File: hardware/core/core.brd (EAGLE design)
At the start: 159.7 x 163.8 mm, 549 parts, among them IC1 MAX481CSA, IC10 MAX481CSA, IC11 MAX481CSA, IC12 MAX481CSA, IC13 MAX481CSA, IC14 MAX481CSA, IC15 MAX481CSA, IC16 MAX481CSA, IC17 MAX481CSA, IC18 MAX481CSA, IC19 MAX481CSA, IC2 LD117AS12TR, IC20 MAX481CSA, IC21 MAX481CSA, IC22 LD117AS12TR, IC23 LD117AS12TR, IC3 MAX481CSA, IC4 MAX481CSA, IC5 MAX481CSA, IC6 MAX481CSA, IC7 MAX481CSA, IC8 MAX481CSA, IC9 MAX481CSA

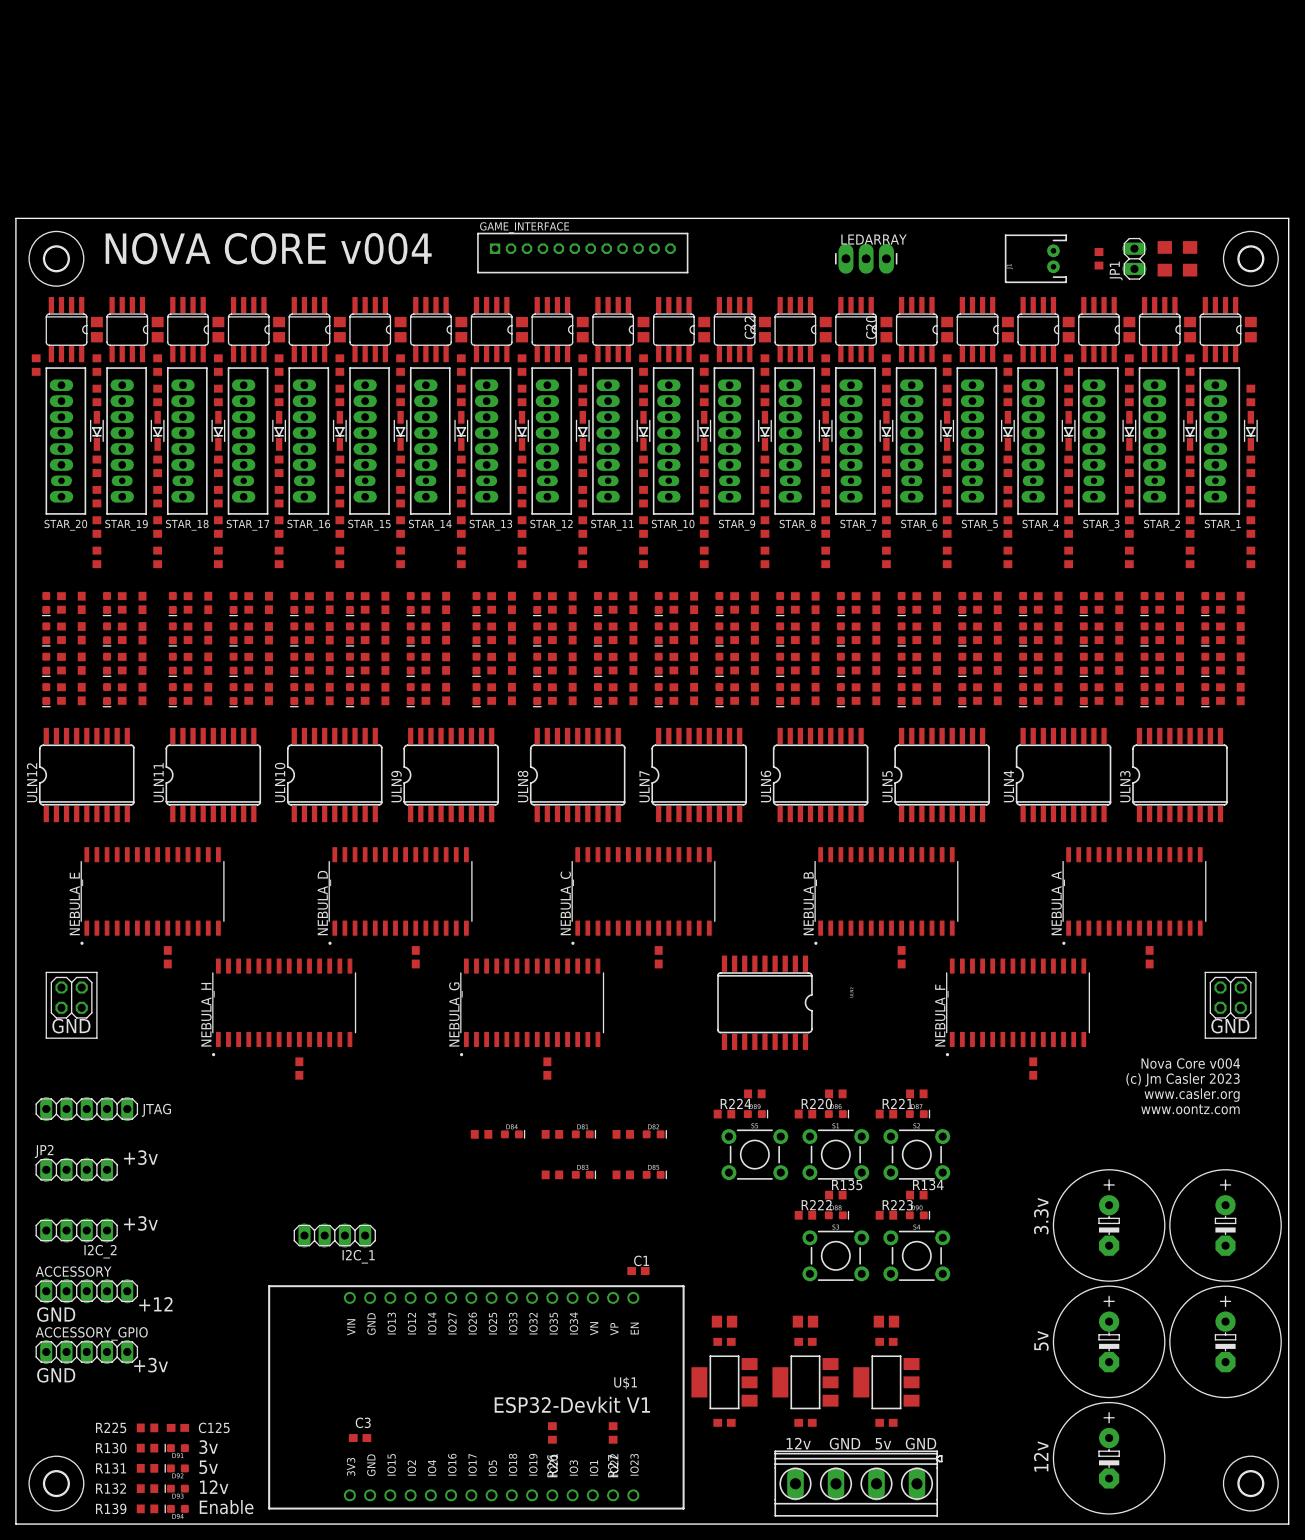
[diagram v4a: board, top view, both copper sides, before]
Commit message: Add TVS and change led resistors to 1k
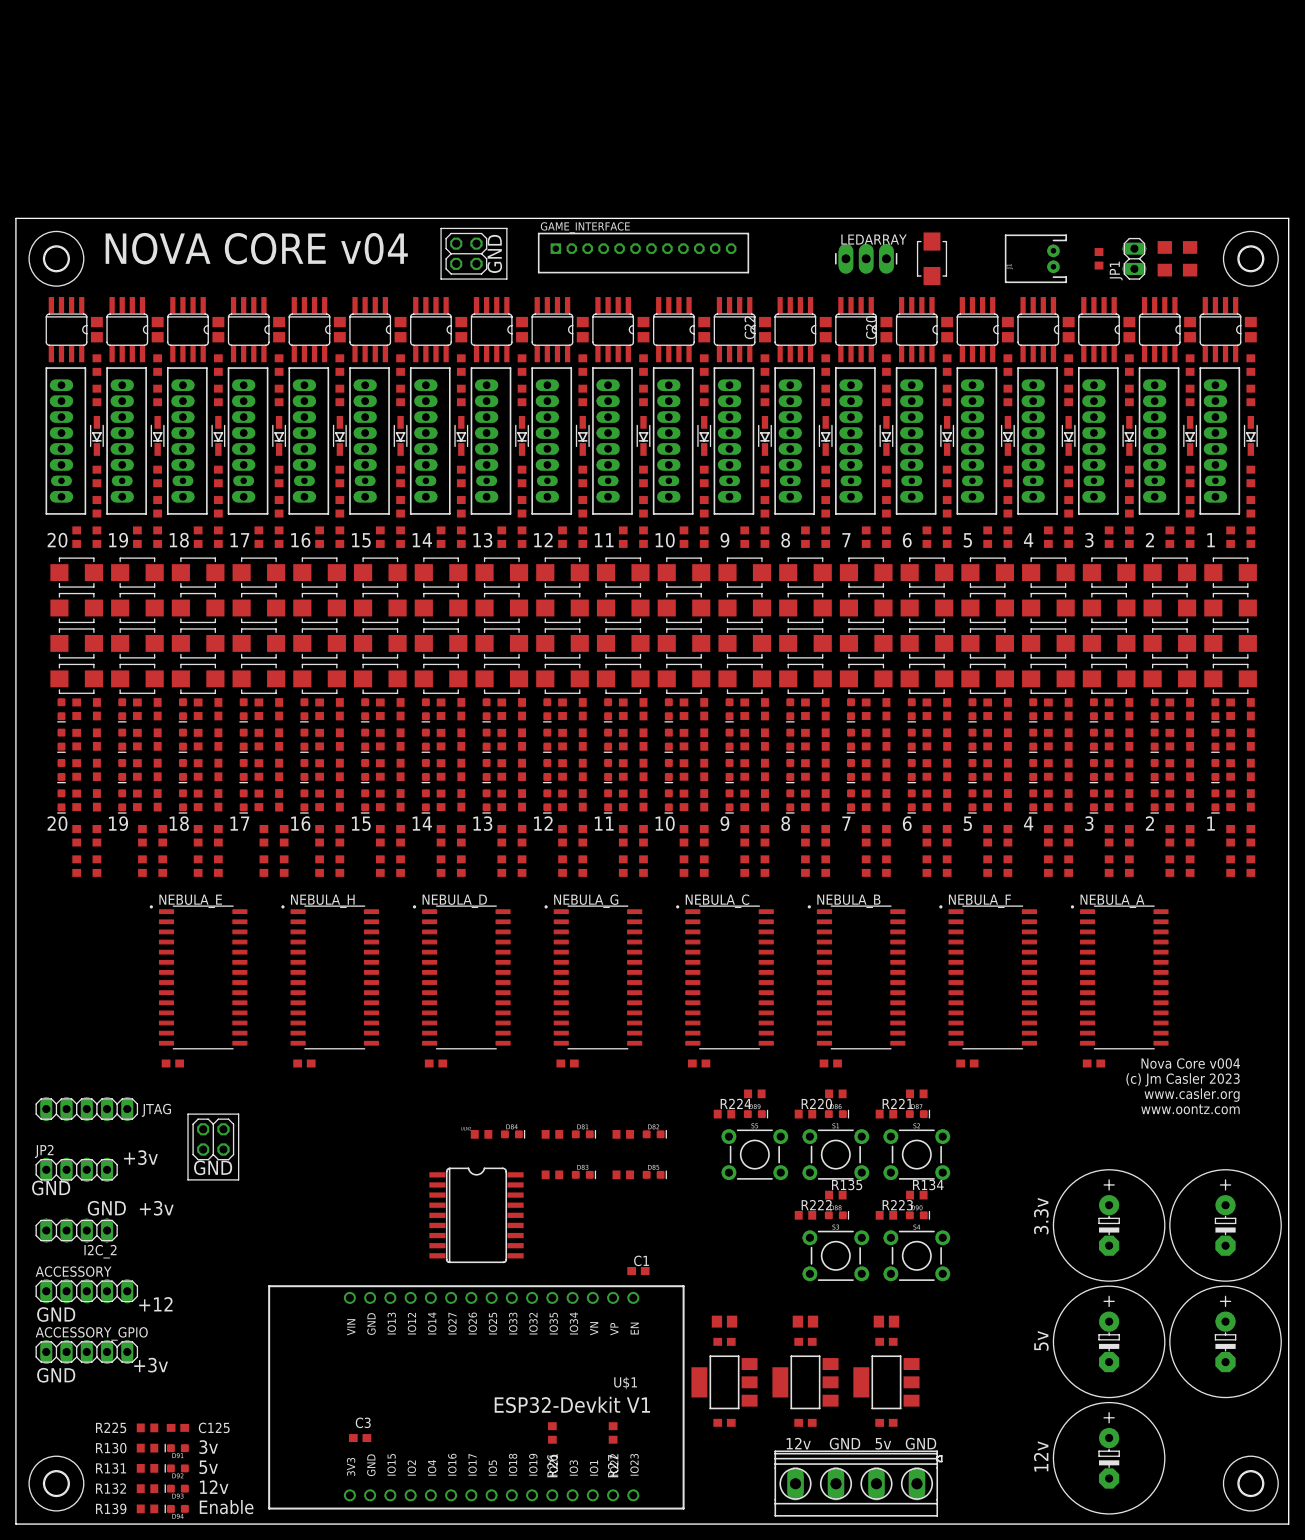
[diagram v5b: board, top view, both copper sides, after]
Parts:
- removed I2C_1: (no value), pinhead:1X04
- removed ULN10, ULN11, ULN12, ULN3, ULN4, ULN5, ULN6, ULN7, ULN8, ULN9: (no value), SparkFun-IC-Special-Function:SO18L
- added D115, D116, D117, D118, D119, D120, D121, D122, D123, D124, D125, D126, D127, D128, D129, D130, D131, D132, D133, D134, D135, D136, D137, D138, D139, D140, D141, D142, D143, D144, D145, D146, D147, D148, D149, D150, D151, D152, D153, D154, D155, D156, D157, D158, D159, D160, D161, D162, D163, D164, D165, D166, D167, D168, D169, D170, D171, D172, D173, D174, D175, D176, D177, D178, D179, D180, D181, D182, D183, D184, D185, D186, D187, D188, D189, D190, D191, D192, D193, D194, D195: SMBJ8.0CA, SMBJ8.0CA:DIOM4336X265N
- added R226, R227, R228, R229, R230, R231, R232, R233, R234, R235, R236, R237, R238, R239, R240, R241, R242, R243, R244, R245, R246, R247, R248, R249, R250, R251, R252, R253, R254, R255, R256, R257, R258, R259, R260, R261, R262, R263, R264, R265, R266, R267, R268, R269, R270, R271, R272, R273, R274, R275, R276, R277, R278, R279, R280, R281, R282, R283, R284, R285, R286, R287, R288, R289, R290, R291, R292, R293, R294, R295, R296, R297, R298, R299, R300, R301, R302, R303, R304, R305: 68, rcl:R0603
- R10, R100, R101, R102, R11, R12, R13, R14, R15, R16, R17, R18, R19, R20, R21, R22, R23, R24, R25, R28, R29, R3, R30, R31, R32, R33, R34, R35, R36, R37, R38, R39, R4, R40, R41, R42, R43, R44, R45, R46, R47, R48, R49, R5, R50, R51, R52, R53, R6, R66, R69, R7, R70, R71, R72, R73, R74, R75, R76, R77, R78, R79, R8, R80, R81, R82, R87, R88, R89, R9, R90, R91, R92, R93, R94, R95, R96, R97, R98, R99: value 10k -> 1k
- moved JP3 133.8 mm to (56.5, 159.4), turned to 90 degrees
- moved ULN2 46.3 mm to (57.8, 43.2), turned to 270 degrees
- moved JP4 25.1 mm to (24.8, 48.3)
- moved C10 16.0 mm to (102.2, 57.8), turned to 180 degrees
- moved NEBULA_C 15.3 mm to (89.5, 68.6), turned to 0 degrees
- moved C8 15.1 mm to (135.3, 57.8), turned to 180 degrees
- moved C9 14.3 mm to (85.7, 57.8), turned to 180 degrees
- moved NEBULA_D 13.6 mm to (56.5, 68.6), turned to 0 degrees
- moved C11 13.6 mm to (52.7, 57.8), turned to 180 degrees
- moved C102 13.5 mm to (55.9, 94.6)
- moved C103 13.5 mm to (55.9, 98.4)
- moved C118 13.5 mm to (17.8, 94.6)
- moved C119 13.5 mm to (17.8, 98.4)
- moved C122 13.5 mm to (10.2, 94.6)
- moved C123 13.5 mm to (10.2, 98.4)
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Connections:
- new net N$345: C45.1, D123.2, R11.1, R151.1, R234.2
- net +12V: no longer ULN10.10, ULN11.10, ULN12.10, ULN3.10, ULN4.10, ULN5.10, ULN6.10, ULN7.10, ULN8.10, ULN9.10
- net +3V3: no longer I2C_1.1
- net +5V: no longer D1.A, D10.A, D11.A, D12.A, D13.A, D14.A, D15.A, D16.A, D17.A, D18.A, D19.A, D2.A, D20.A, D21.A, D22.A, D23.A, D24.A, D25.A, D26.A, D27.A, D28.A, D29.A, D3.A, D30.A, D31.A, D32.A, D33.A, D34.A, D35.A, D36.A, D37.A, D38.A, D39.A, D4.A, D40.A, D41.A, D42.A, D43.A, D44.A, D45.A, D46.A, D47.A, D48.A, D49.A, D5.A, D50.A, D51.A, D52.A, D53.A, D54.A, D55.A, D56.A, D57.A, D58.A, D59.A, D6.A, D60.A, D61.A, D62.A, D63.A, D64.A, D65.A, D66.A, D67.A, D68.A, D69.A, D7.A, D70.A, D71.A, D72.A, D73.A, D74.A, D75.A, D76.A, D77.A, D78.A, D79.A, D8.A, D80.A, D9.A
- net 21/SDA: no longer I2C_1.4
- net 22/SCL: no longer I2C_1.3
- net A0: now also R226.1; no longer ULN3.8
- net A1: now also R227.1; no longer ULN3.7
- net A10: now also R236.1; no longer ULN4.6
- net A11: now also R237.1; no longer ULN4.5
- net A12: now also R238.1; no longer ULN4.4
- net A13: now also R239.1; no longer ULN4.3
- net A14: now also R240.1; no longer ULN4.2
- net A15: now also R241.1; no longer ULN4.1
- net A2: now also R228.1; no longer ULN3.6
- net A3: now also R229.1; no longer ULN3.5
- net A4: now also R230.1; no longer ULN3.4
- net A5: now also R231.1; no longer ULN3.3
- net A6: now also R232.1; no longer ULN3.2
- net A7: now also R233.1; no longer ULN3.1
- net A8: now also R234.1; no longer ULN4.8
- net A9: now also R235.1; no longer ULN4.7
- net B0: now also R242.1; no longer ULN5.8
- net B1: now also R243.1; no longer ULN5.7
- net B10: now also R252.1; no longer ULN6.6
- net B11: now also R253.1; no longer ULN6.5
- net B12: now also R254.1; no longer ULN6.4
- net B13: now also R255.1; no longer ULN6.3
- net B14: now also R256.1; no longer ULN6.2
- net B15: now also R257.1; no longer ULN6.1
- net B2: now also R244.1; no longer ULN5.6
- net B3: now also R245.1; no longer ULN5.5
- net B4: now also R246.1; no longer ULN5.4
- net B5: now also R247.1; no longer ULN5.3
- net B6: now also R248.1; no longer ULN5.2
- net B7: now also R249.1; no longer ULN5.1
- net B8: now also R250.1; no longer ULN6.8
- net B9: now also R251.1; no longer ULN6.7
- net C0: now also R258.1; no longer ULN7.8
- net C1: now also R259.1; no longer ULN7.7
- net C10: now also R268.1; no longer ULN8.6
- net C11: now also R269.1; no longer ULN8.5
- net C12: now also R270.1; no longer ULN8.4
- net C13: now also R271.1; no longer ULN8.3
- net C14: now also R272.1; no longer ULN8.2
- net C15: now also R273.1; no longer ULN8.1
- net C2: now also R260.1; no longer ULN7.6
- net C3: now also R261.1; no longer ULN7.5
- net C4: now also R262.1; no longer ULN7.4
- net C5: now also R263.1; no longer ULN7.3
- net C6: now also R264.1; no longer ULN7.2
- net C7: now also R265.1; no longer ULN7.1
- net C8: now also R266.1; no longer ULN8.8
- net C9: now also R267.1; no longer ULN8.7
- net D0: now also R274.1; no longer ULN9.8
- net D1: now also R275.1; no longer ULN9.7
- net D10: now also R284.1; no longer ULN10.6
- net D11: now also R285.1; no longer ULN10.5
- net D12: now also R286.1; no longer ULN10.4
- net D13: now also R287.1; no longer ULN10.3
- net D14: now also R288.1; no longer ULN10.2
- net D15: now also R289.1; no longer ULN10.1
- net D2: now also R276.1; no longer ULN9.6
- net D3: now also R277.1; no longer ULN9.5
- net D4: now also R278.1; no longer ULN9.4
- net D5: now also R279.1; no longer ULN9.3
- net D6: now also R280.1; no longer ULN9.2
- net D7: now also R281.1; no longer ULN9.1
- net D8: now also R282.1; no longer ULN10.8
- net D9: now also R283.1; no longer ULN10.7
- net E0: now also R290.1; no longer ULN11.8
- net E1: now also R291.1; no longer ULN11.7
- net E10: now also R300.1; no longer ULN12.6
- net E11: now also R301.1; no longer ULN12.5
- net E12: now also R302.1; no longer ULN12.4
- net E13: now also R303.1; no longer ULN12.3
- net E14: now also R304.1; no longer ULN12.2
- net E15: now also R305.1; no longer ULN12.1
- net E2: now also R292.1; no longer ULN11.6
- net E3: now also R293.1; no longer ULN11.5
- net E4: now also R294.1; no longer ULN11.4
- net E5: now also R295.1; no longer ULN11.3
- net E6: now also R296.1; no longer ULN11.2
- net E7: now also R297.1; no longer ULN11.1
- net E8: now also R298.1; no longer ULN12.8
- net E9: now also R299.1; no longer ULN12.7
- net GND: now also D10.C, D11.C, D115.1, D116.1, D117.1, D118.1, D119.1, D12.C, D120.1, D121.1, D122.1, D123.1, D124.1, D125.1, D126.1, D127.1, D128.1, D129.1, D13.C, D130.1, D131.1, D132.1, D133.1, D134.1, D135.1, D136.1, D137.1, D138.1, D139.1, D14.C, D140.1, D141.1, D142.1, D143.1, D144.1, D145.1, D146.1, D147.1, D148.1, D149.1, D15.C, D150.1, D151.1, D152.1, D153.1, D154.1, D155.1, D156.1, D157.1, D158.1, D159.1, D16.C, D160.1, D161.1, D162.1, D163.1, D164.1, D165.1, D166.1, D167.1, D168.1, D169.1, D17.C, D170.1, D171.1, D172.1, D173.1, D174.1, D175.1, D176.1, D177.1, D178.1, D179.1, D18.C, D180.1, D181.1, D182.1, D183.1, D184.1, D185.1, D186.1, D187.1, D188.1, D189.1, D19.C, D190.1, D191.1, D192.1, D193.1, D194.1, D195.1, D2.C, D20.C, D21.C, D22.C, D23.C, D24.C, D25.C, D26.C, D27.C, D28.C, D29.C, D3.C, D30.C, D31.C, D32.C, D33.C, D34.C, D35.C, D36.C, D37.C, D38.C, D39.C, D4.C, D40.C, D41.C, D42.C, D43.C, D44.C, D45.C, D46.C, D47.C, D48.C, D49.C, D5.C, D57.C, D58.C, D59.C, D6.C, D60.C, D61.C, D62.C, D63.C, D64.C, D65.C, D66.C, D67.C, D68.C, D69.C, D7.C, D70.C, D71.C, D72.C, D73.C, D74.C, D75.C, D76.C, D77.C, D78.C, D79.C, D8.C, D80.C, D9.C; no longer I2C_1.2, ULN10.9, ULN11.9, ULN12.9, ULN3.9, ULN4.9, ULN5.9, ULN6.9, ULN7.9, ULN8.9, ULN9.9
- net N$100: now also D69.A, R91.2; no longer D77.C, R99.2
- net N$101: now also D70.A, R92.2; no longer D78.C, R100.2
- net N$102: now also D71.A, R93.2; no longer D79.C, R101.2
- net N$103: now also D72.A, R94.2; no longer D80.C, R102.2
- net N$11: now also D6.A; no longer D6.C
- net N$12: now also D7.A; no longer D7.C
- net N$13: now also D8.A; no longer D8.C
- net N$14: now also D9.A; no longer D9.C
- net N$160: now also D116.2, R226.2; no longer ULN3.11
- net N$161: now also D115.2, R227.2; no longer ULN3.12
- net N$162: now also D117.2, R228.2; no longer ULN3.13
- net N$163: now also D118.2, R229.2; no longer ULN3.14
- net N$164: now also D122.2, R233.2; no longer ULN3.18
- net N$165: now also D121.2, R232.2; no longer ULN3.17
- net N$166: now also D120.2, R231.2; no longer ULN3.16
- net N$167: now also D119.2, R230.2; no longer ULN3.15
- net N$184: now also D49.A, R52.2; no longer C45.1, R11.1, R151.1, ULN4.11
- net N$185: now also D124.2, R235.2; no longer ULN4.12
- net N$186: now also D125.2, R236.2; no longer ULN4.13
- net N$187: now also D126.2, R237.2; no longer ULN4.14
- net N$188: now also D130.2, R241.2; no longer ULN4.18
- net N$189: now also D129.2, R240.2; no longer ULN4.17
- net N$190: now also D128.2, R239.2; no longer ULN4.16
- net N$191: now also D127.2, R238.2; no longer ULN4.15
- net N$192: now also D131.2, R242.2; no longer ULN5.11
- net N$193: now also D134.2, R245.2; no longer ULN5.14
- net N$194: now also D133.2, R244.2; no longer ULN5.13
- net N$195: now also D132.2, R243.2; no longer ULN5.12
- net N$196: now also D138.2, R249.2; no longer ULN5.18
- net N$197: now also D137.2, R248.2; no longer ULN5.17
- net N$198: now also D136.2, R247.2; no longer ULN5.16
- net N$199: now also D135.2, R246.2; no longer ULN5.15
- net N$20: now also D14.A, R15.2; no longer D10.C, R11.2
- net N$21: now also D15.A, R16.2; no longer D11.C, R12.2
- net N$216: now also D139.2, R250.2; no longer ULN6.11
- net N$217: now also D140.2, R251.2; no longer ULN6.12
- net N$218: now also D141.2, R252.2; no longer ULN6.13
- net N$219: now also D142.2, R253.2; no longer ULN6.14
- net N$22: now also D16.A, R17.2; no longer D12.C, R13.2
- net N$220: now also D146.2, R257.2; no longer ULN6.18
- net N$221: now also D145.2, R256.2; no longer ULN6.17
- net N$222: now also D144.2, R255.2; no longer ULN6.16
- net N$223: now also D143.2, R254.2; no longer ULN6.15
- net N$23: now also D17.A, R18.2; no longer D13.C, R14.2
- net N$240: now also D147.2, R258.2; no longer ULN7.11
- net N$241: now also D148.2, R259.2; no longer ULN7.12
- net N$242: now also D149.2, R260.2; no longer ULN7.13
- net N$243: now also D150.2, R261.2; no longer ULN7.14
- net N$245: now also D153.2, R264.2; no longer ULN7.17
- net N$246: now also D152.2, R263.2; no longer ULN7.16
- net N$247: now also D151.2, R262.2; no longer ULN7.15
- net N$248: now also D155.2, R266.2; no longer ULN8.11
- net N$249: now also D156.2, R267.2; no longer ULN8.12
- net N$250: now also D157.2, R268.2; no longer ULN8.13
- net N$251: now also D158.2, R269.2; no longer ULN8.14
- net N$252: now also D154.2, R265.2; no longer ULN7.18
- net N$253: now also D161.2, R272.2; no longer ULN8.17
- net N$254: now also D160.2, R271.2; no longer ULN8.16
- net N$255: now also D159.2, R270.2; no longer ULN8.15
- net N$26: now also D56.A, R74.2; no longer D1.C, R53.2
- net N$260: now also D162.2, R273.2; no longer ULN8.18
- net N$27: now also D55.A, R73.2; no longer D50.C, R66.2
- net N$28: now also D13.A, R14.2; no longer D14.C, R15.2
- net N$288: now also D172.2, R282.2; no longer ULN10.11
- net N$289: now also D173.2, R283.2; no longer ULN10.12
- net N$29: now also D12.A, R13.2; no longer D15.C, R16.2
- net N$290: now also D174.2, R284.2; no longer ULN10.13
- net N$291: now also D175.2, R285.2; no longer ULN10.14
- net N$292: now also D179.2, R289.2; no longer ULN10.18
- net N$293: now also D178.2, R288.2; no longer ULN10.17
- net N$294: now also D177.2, R287.2; no longer ULN10.16
- net N$295: now also D176.2, R286.2; no longer ULN10.15
- net N$296: now also D163.2, R274.2; no longer ULN9.11
- net N$297: now also D164.2, R275.2; no longer ULN9.12
- net N$298: now also D165.2, R276.2; no longer ULN9.13
- net N$299: now also D166.2, R277.2; no longer ULN9.14
- net N$3: now also D2.A; no longer D2.C
- net N$30: now also D11.A, R12.2; no longer D16.C, R17.2
- net N$300: now also D170.2, R281.2; no longer ULN9.18
- net N$301: now also D169.2, R280.2; no longer ULN9.17
- net N$302: now also D168.2, R279.2; no longer ULN9.16
- net N$303: now also D167.2, R278.2; no longer ULN9.15
- net N$304: now also D180.2, R290.2; no longer ULN11.11
- net N$305: now also D181.2, R291.2; no longer ULN11.12
- net N$306: now also D182.2, R292.2; no longer ULN11.13
- net N$307: now also D183.2, R293.2; no longer ULN11.14
- net N$308: now also D187.2, R297.2; no longer ULN11.18
- net N$309: now also D186.2, R296.2; no longer ULN11.17
- net N$31: now also D10.A, R11.2; no longer D17.C, R18.2
- net N$310: now also D185.2, R295.2; no longer ULN11.16
- net N$311: now also D184.2, R294.2; no longer ULN11.15
- net N$312: now also D188.2, R298.2; no longer ULN12.11
- net N$313: now also D189.2, R299.2; no longer ULN12.12
- net N$314: now also D190.2, R300.2; no longer ULN12.13
- net N$315: now also D191.2, R301.2; no longer ULN12.14
- net N$316: now also D195.2, R305.2; no longer ULN12.18
- net N$317: now also D194.2, R304.2; no longer ULN12.17
- net N$318: now also D193.2, R303.2; no longer ULN12.16
- net N$319: now also D192.2, R302.2; no longer ULN12.15
- net N$32: now also D54.A, R72.2; no longer D51.C, R69.2
- net N$33: now also D53.A, R71.2; no longer D52.C, R70.2
- net N$34: now also D80.A, R102.2; no longer D65.C, R87.2
- net N$35: now also D1.A, R53.2; no longer D53.C, R71.2
- net N$36: now also D25.A, R28.2; no longer D18.C, R19.2
- net N$37: now also D24.A, R25.2; no longer D19.C, R20.2
- net N$38: now also D23.A, R24.2; no longer D20.C, R21.2
- net N$39: now also D22.A, R23.2; no longer D21.C, R22.2
- net N$4: now also D3.A; no longer D3.C
- net N$40: now also D50.A, R66.2; no longer D54.C, R72.2
- net N$41: now also D51.A, R69.2; no longer D55.C, R73.2
- net N$42: now also D52.A, R70.2; no longer D56.C, R74.2
- net N$43: now also D61.A, R79.2; no longer D57.C, R75.2
- net N$44: now also D21.A, R22.2; no longer D22.C, R23.2
- net N$45: now also D20.A, R21.2; no longer D23.C, R24.2
- net N$46: now also D19.A, R20.2; no longer D24.C, R25.2
- net N$47: now also D18.A, R19.2; no longer D25.C, R28.2
- net N$48: now also D62.A, R80.2; no longer D58.C, R76.2
- net N$49: now also D63.A, R81.2; no longer D59.C, R77.2
- net N$5: now also D4.A; no longer D4.C
- net N$50: now also D64.A, R82.2; no longer D60.C, R78.2
- net N$52: now also D26.A; no longer D26.C
- net N$53: now also D27.A; no longer D27.C
- net N$54: now also D28.A; no longer D28.C
- net N$55: now also D29.A; no longer D29.C
- net N$6: now also D5.A; no longer D5.C
- net N$60: now also D30.A; no longer D30.C
- net N$61: now also D31.A; no longer D31.C
- net N$62: now also D32.A; no longer D32.C
- net N$63: now also D33.A; no longer D33.C
- net N$64: now also D57.A, R75.2; no longer D61.C, R79.2
- net N$65: now also D58.A, R76.2; no longer D62.C, R80.2
- net N$66: now also D59.A, R77.2; no longer D63.C, R81.2
- net N$67: now also D60.A, R78.2; no longer D64.C, R82.2
- net N$68: now also D34.A; no longer D34.C
- net N$69: now also D35.A; no longer D35.C
- net N$70: now also D36.A; no longer D36.C
- net N$71: now also D37.A; no longer D37.C
- net N$76: now also D38.A; no longer D38.C
- net N$77: now also D39.A; no longer D39.C
- net N$78: now also D40.A; no longer D40.C
- net N$79: now also D41.A; no longer D41.C
- net N$80: now also D79.A, R101.2; no longer D66.C, R88.2
- net N$81: now also D78.A, R100.2; no longer D67.C, R89.2
- net N$82: now also D77.A, R99.2; no longer D68.C, R90.2
- net N$83: now also D76.A, R98.2; no longer D69.C, R91.2
- net N$84: now also D1.C, D50.C, D51.C, D52.C, D53.C, D54.C, D55.C, D56.C; no longer D42.C, R45.2
- net N$85: now also D42.A, R45.2; no longer D43.C, R46.2
- net N$86: now also D43.A, R46.2; no longer D44.C, R47.2
- net N$87: now also D44.A, R47.2; no longer D45.C, R48.2
- net N$88: now also D75.A, R97.2; no longer D70.C, R92.2
- net N$90: now also D74.A, R96.2; no longer D71.C, R93.2
- net N$91: now also D73.A, R95.2; no longer D72.C, R94.2
- net N$92: now also D65.A, R87.2; no longer D73.C, R95.2
- net N$93: now also D45.A, R48.2; no longer D46.C, R49.2
- net N$94: now also D46.A, R49.2; no longer D47.C, R50.2
- net N$95: now also D47.A, R50.2; no longer D48.C, R51.2
- net N$96: now also D48.A, R51.2; no longer D49.C, R52.2
- net N$97: now also D66.A, R88.2; no longer D74.C, R96.2
- net N$98: now also D67.A, R89.2; no longer D75.C, R97.2
- net N$99: now also D68.A, R90.2; no longer D76.C, R98.2
- net STAR_ENABLE: now also D171.2
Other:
- board text added: "1"
- board text added: "10"
- board text added: "11"
- board text added: "12"
- board text added: "13"
- board text added: "14"
- board text added: "15"
- board text added: "16"
- board text added: "17"
- board text added: "18"
- board text added: "19"
- board text added: "2"
- board text added: "20"
- board text added: "3"
- board text added: "4"
- board text added: "5"
- board text added: "6"
- board text added: "7"
- board text added: "8"
- board text added: "9"
- board text added: "GND +3v"
- board text added: "NOVA CORE v04"
- board text removed: "NOVA CORE v004"

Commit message: misc board updates
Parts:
- removed LEDARRAY: (no value), SparkFun-Connectors:1X03_LONGPADS
- added APA102: (no value), pinhead:1X04
- added D196, D197: SMBJ8.0CA, SMBJ8.0CA:DIOM4336X265N
- moved POWER_IN 51.8 mm to (154.3, 22.2), turned to 270 degrees
- moved C69 10.2 mm to (141.6, 22.9)
- moved C70 10.2 mm to (141.6, 37.5)
- moved C71 10.2 mm to (127.0, 22.9)
- moved C72 10.2 mm to (127.0, 37.5)
- moved C89 10.2 mm to (127.0, 8.26)
- moved D86 2.54 mm to (100.3, 51.4)
- moved D87 2.54 mm to (110.5, 51.4)
- moved D88 2.54 mm to (100.3, 38.7)
- moved D90 2.54 mm to (110.5, 38.7)
- moved R134 2.54 mm to (110.5, 41.3)
- moved R135 2.54 mm to (100.3, 41.3)
- moved R136 2.54 mm to (110.5, 54.0)
- moved R137 2.54 mm to (100.3, 54.0)
- moved R220 2.54 mm to (96.5, 51.4)
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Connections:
- net +5V: now also APA102.4; no longer LEDARRAY.3
- net 18: now also APA102.2, D197.2
- net 4: now also APA102.3, D196.2; no longer LEDARRAY.2
- net GND: now also APA102.1, D196.1, D197.1; no longer LEDARRAY.1
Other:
- board text added: "GND p18 p4 +5"
- board text removed: "+5 DATA GND"

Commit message: updates
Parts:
- removed C90: 1uf, rcl:C0805
- removed C91, C92: 10uf, rcl:C0603
- removed IC23: LD117AS12TR, v-reg:SOT223
- removed J1: (no value), SparkFun-Connectors:JST-2-PTH
- removed JP1: (no value), pinhead:1X02
- added C126, C127: C_100NF/50V_0603, JLC PCB Basic Parts_loc:C0603
- added C130: 1uf, rcl:C0805
- added D198: D_B5819W-SL_CHANGJ_SOD123, JLC PCB Basic Parts_loc:SOD123
- added ESTOP: B2B-PH-K, con-jst-ph:B2B-PH-K
- added ESTOP_2: (no value), pinhead:1X02
- added MIDI: B4B-PH-K, con-jst-ph:B4B-PH-K
- added R306, R307: R_220R_0603, JLC PCB Basic Parts_loc:R0603
- added R310: R_1K_0603, JLC PCB Basic Parts_loc:R0603
- added U1: 6N138SDM, 6N138SDM:COUPL_6N138SDM
- APA102: value (none) -> B4B-PH-K; device pinhead:1X04 -> con-jst-ph:B4B-PH-K
- C100, C101, C102, C103, C104, C105, C106, C107, C108, C109, C110, C111, C112, C113, C114, C115, C116, C117, C118, C119, C120, C121, C122, C123, C37, C38, C39, C40, C41, C42, C43, C44, C45, C46, C47, C48, C49, C50, C51, C52, C53, C54, C55, C56, C57, C58, C59, C60, C61, C62, C63, C64, C65, C66, C67, C68, C73, C74, C75, C76, C77, C78, C79, C80, C81, C82, C83, C84, C85, C86, C87, C88, C93, C94, C95, C96, C97, C98, C99: value 1nf -> 100nf
- moved JP4 123.5 mm to (141.6, 8.26)
- moved ULN2 30.6 mm to (34.9, 63.5)
- moved JP3 27.9 mm to (67.9, 184.8), turned to 0 degrees
- moved APA102 27.0 mm to (110.5, 184.8)
- moved D196 26.3 mm to (118.7, 184.2)
- moved D197 26.3 mm to (102.2, 184.2)
- moved D171 26.2 mm to (123.8, 184.2)
- moved GAME_INTERFACE 25.7 mm to (85.7, 184.8)
- moved C10 25.4 mm to (102.2, 83.2)
- moved C100 25.4 mm to (48.3, 127.6)
- moved C102 25.4 mm to (55.9, 120.0)
- moved C103 25.4 mm to (55.9, 123.8)
- moved C104 25.4 mm to (55.9, 127.6)
- moved C106 25.4 mm to (40.6, 120.0)
- moved C107 25.4 mm to (40.6, 123.8)
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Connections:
- new net N$347: D198.A, R306.2, U1.3
- new net N$348: C126.1, MIDI.1
- new net N$349: C127.1, MIDI.2
- new net N$352: MIDI.3, R306.1
- new net N$353: D198.C, MIDI.4, U1.2
- net +12V: now also C35.1, C6.1, IC22.3; no longer C90.1, C92.1, IC23.3
- net +3V3: now also R307.2
- net +5V: now also C130.1, U1.8; no longer C35.1, C6.1, C91.1, IC22.3, IC23.4
- net 19: now also R307.1, R310.1, R310.2, U1.6
- net GND: now also C126.2, C127.2, C130.2, U1.5; no longer C90.2, C91.2, C92.2, IC23.1
- net N$89: now also ESTOP.2, ESTOP_2.2; no longer J1.2, JP1.2
- net STAR_ENABLE: now also ESTOP.1, ESTOP_2.1; no longer J1.1, JP1.1
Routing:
- net +12V: track 0.00 -> 230.0 mm
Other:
- board size 159.7 x 163.8 mm -> 159.7 x 189.2 mm
- board text added: "Nova: Core"
- board text removed: "NOVA CORE v04"

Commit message: partially routed
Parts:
- added C90: 2200uf, rcl:E5-13
- added F1, F2: MF-MSMF-STYLE2_1, Fuse:FUSC4632X160
- moved C71 35.3 mm to (136.5, 56.5)
- moved C72 35.3 mm to (136.5, 71.1)
- moved C69 35.3 mm to (151.1, 56.5)
- moved C70 35.3 mm to (151.1, 71.1)
- moved C89 35.3 mm to (136.5, 41.9)
- moved I2C_2 1.91 mm to (9.53, 36.8)
- moved JP2 1.91 mm to (9.53, 44.5)
- moved ACCESSORY 1.90 mm to (10.8, 29.2)
- moved ACCESSORY_GPIO 1.90 mm to (10.8, 21.6)
- moved JTAG 1.90 mm to (10.8, 52.1)
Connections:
- new net +14V: C90.+, F2.2, GAME_INTERFACE.12
- new net N$346: F1.1, F2.1, POWER_IN.4
- net +12V: now also F1.2; no longer GAME_INTERFACE.12, POWER_IN.4
- net GND: now also C90.-
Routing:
- net 17: track 0.00 -> 376.4 mm
- net 16: track 0.00 -> 371.2 mm
- net +5V: track 0.00 -> 351.3 mm
- net +3V3: track 0.00 -> 266.8 mm
- net +14V: track 0.00 -> 231.7 mm
- net +12V: track 230.0 -> 92.9 mm
- net GND: track 0.00 -> 77.4 mm
- net N$346: track 0.00 -> 13.5 mm
- net N$7: track 0.00 -> 6.75 mm
- net N$330: track 0.00 -> 6.75 mm
- net N$19: track 0.00 -> 6.75 mm
- net N$105: track 0.00 -> 6.75 mm
- net N$338: track 0.00 -> 6.75 mm
- net N$344: track 0.00 -> 6.75 mm
- net N$340: track 0.00 -> 6.75 mm
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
